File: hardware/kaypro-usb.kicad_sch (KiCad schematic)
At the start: 13 parts, among them J1 USB_A, J2 RJ11, U1 Pico, U2 6N137

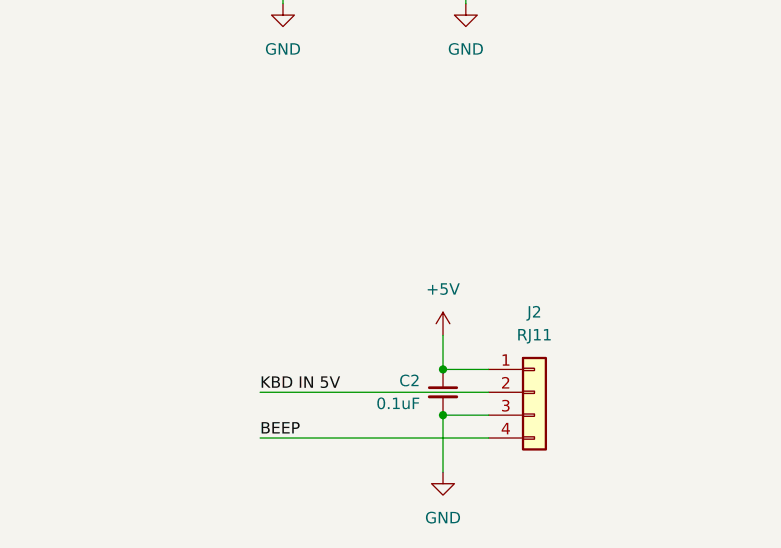
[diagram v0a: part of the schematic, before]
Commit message: Added diode to prevent USB power leaking to the Kaypro when debugging.
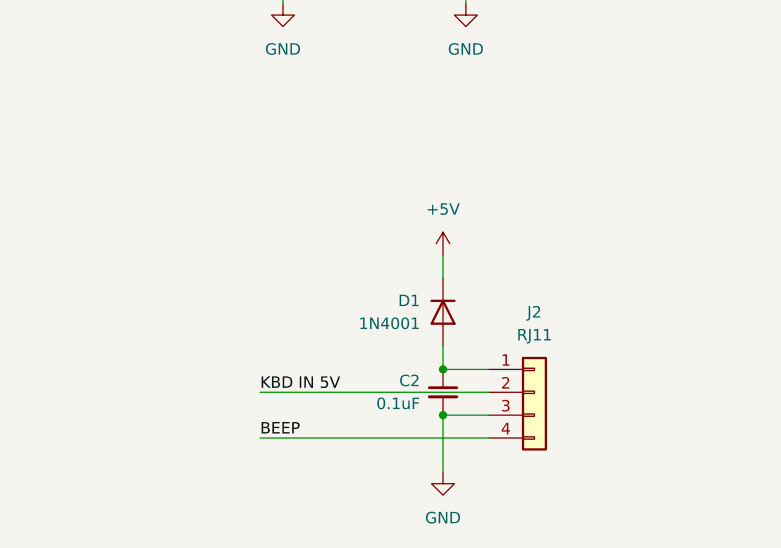
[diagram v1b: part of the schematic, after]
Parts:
- added D1: 1N4001, Diode_THT:D_DO-41_SOD81_P10.16mm_Horizontal, symbol Diode:1N4001
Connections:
- net +5V: now also D1.1 (K); no longer C2.1, J2.1 (Pin_1)
- new net: C2.1, D1.2 (A), J2.1 (Pin_1)
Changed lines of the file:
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@@
+    (stroke (width 0) (type default))
+  )
+  (wire (pts (xy 208.28 118.11) (xy 208.28 120.65))
     (stroke (width 0) (type default))
   )
@@
     (stroke (width 0) (type default))
   )
-  (wire (pts (xy 208.28 127) (xy 208.28 130.81))
+  (wire (pts (xy 208.28 128.27) (xy 208.28 130.81))
     (stroke (width 0) (type default))
   )
@@
     )
   )
-  (symbol (lib_id "power:+5V") (at 208.28 127 0) (mirror y) (unit 1)
-    (in_bom yes) (on_board yes) (dnp no) (fields_autoplaced)
-    (property "Reference" "#PWR013" (at 208.28 130.81 0)
-      (effects (font (size 1.27 1.27)) hide)
-    )
-    (property "Value" "+5V" (at 208.28 121.92 0)
-      (effects (font (size 1.27 1.27)))
-    )
-    (property "Footprint" "" (at 208.28 127 0)
-      (effects (font (size 1.27 1.27)) hide)
-    )
-    (property "Datasheet" "" (at 208.28 127 0)
-      (effects (font (size 1.27 1.27)) hide)
-    )
-    (pin "1")
-    (instances
-      (project "kaypro-usb"
-        (path "/8e4f5c4f-9047-42d1-bb0a-6e8ae15833be"
-          (reference "#PWR013") (unit 1)
-        )
-      )
-    )
-  )
   (symbol (lib_id "power:GND") (at 208.28 142.24 0) (mirror y) (unit 1)
     (in_bom yes) (on_board yes) (dnp no) (fields_autoplaced)
@@
     )
   )
+  (symbol (lib_id "power:+5V") (at 208.28 118.11 0) (mirror y) (unit 1)
+    (in_bom yes) (on_board yes) (dnp no) (fields_autoplaced)
+    (property "Reference" "#PWR013" (at 208.28 121.92 0)
+      (effects (font (size 1.27 1.27)) hide)
+    )
+    (property "Value" "+5V" (at 208.28 113.03 0)
+      (effects (font (size 1.27 1.27)))
+    )
+    (property "Footprint" "" (at 208.28 118.11 0)
+      (effects (font (size 1.27 1.27)) hide)
+    )
+    (property "Datasheet" "" (at 208.28 118.11 0)
+      (effects (font (size 1.27 1.27)) hide)
+    )
+    (pin "1")
+    (instances
+      (project "kaypro-usb"
+        (path "/8e4f5c4f-9047-42d1-bb0a-6e8ae15833be"
+          (reference "#PWR013") (unit 1)
+        )
+      )
+    )
+  )
   (symbol (lib_id "power:+3V3") (at 128.27 67.31 0) (unit 1)
     (in_bom yes) (on_board yes) (dnp no) (fields_autoplaced)
@@
         )
       )
+    )
+  )
+  (symbol (lib_id "Diode:1N4001") (at 208.28 124.46 270) (unit 1)
+    (in_bom yes) (on_board yes) (dnp no)
+    (property "Reference" "D1" (at 205.74 123.19 90)
+      (effects (font (size 1.27 1.27)) (justify right))
+    )
+    (property "Value" "1N4001" (at 205.74 125.73 90)
+      (effects (font (size 1.27 1.27)) (justify right))
+    )
+    (property "Footprint" "Diode_THT:D_DO-41_SOD81_P10.16mm_Horizontal" (at 208.28 124.46 0)
+      (effects (font (size 1.27 1.27)) hide)
+    )
+    (property "Datasheet" "http://www.vishay.com/docs/88503/1n4001.pdf" (at 208.28 124.46 0)
+      (effects (font (size 1.27 1.27)) hide)
+    )
+    (property "Sim.Device" "D" (at 208.28 124.46 0)
+      (effects (font (size 1.27 1.27)) hide)
+    )
+    (property "Sim.Pins" "1=K 2=A" (at 208.28 124.46 0)
+      (effects (font (size 1.27 1.27)) hide)
+    )
+    (pin "1")
+    (pin "2")
+    (instances
+      (project "kaypro-usb"
+        (path "/8e4f5c4f-9047-42d1-bb0a-6e8ae15833be"
+          (reference "D1") (unit 1)
+        )
+      )
